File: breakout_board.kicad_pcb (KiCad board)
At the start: 2 copper layers, 30 x 27.6 mm, 27 parts, among them IC2 AS5600-ASOT, J1 Dummy Pins, J2 Debugger, J3 USB_C, U1 STM32F103C8Tx, U2 AMS1117-3.3, Y2 Crystal

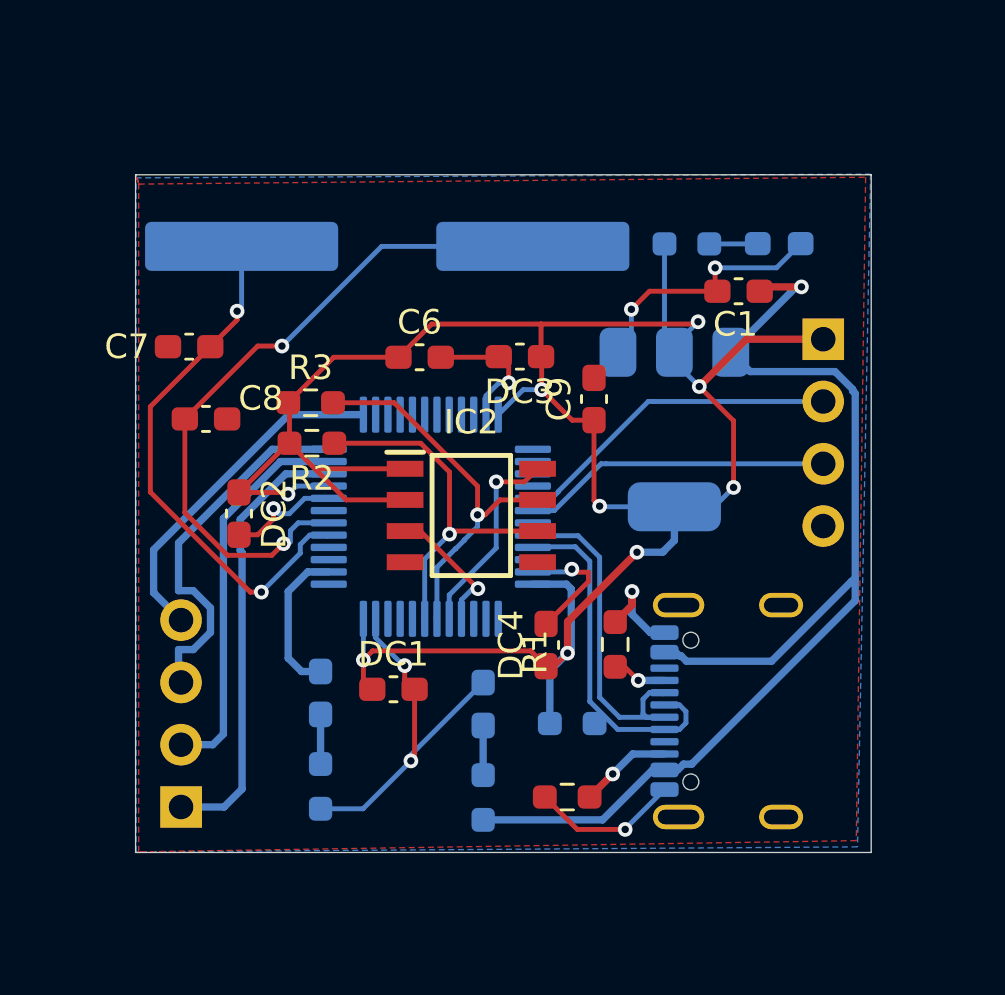
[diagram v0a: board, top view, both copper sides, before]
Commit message: added return vias for ground
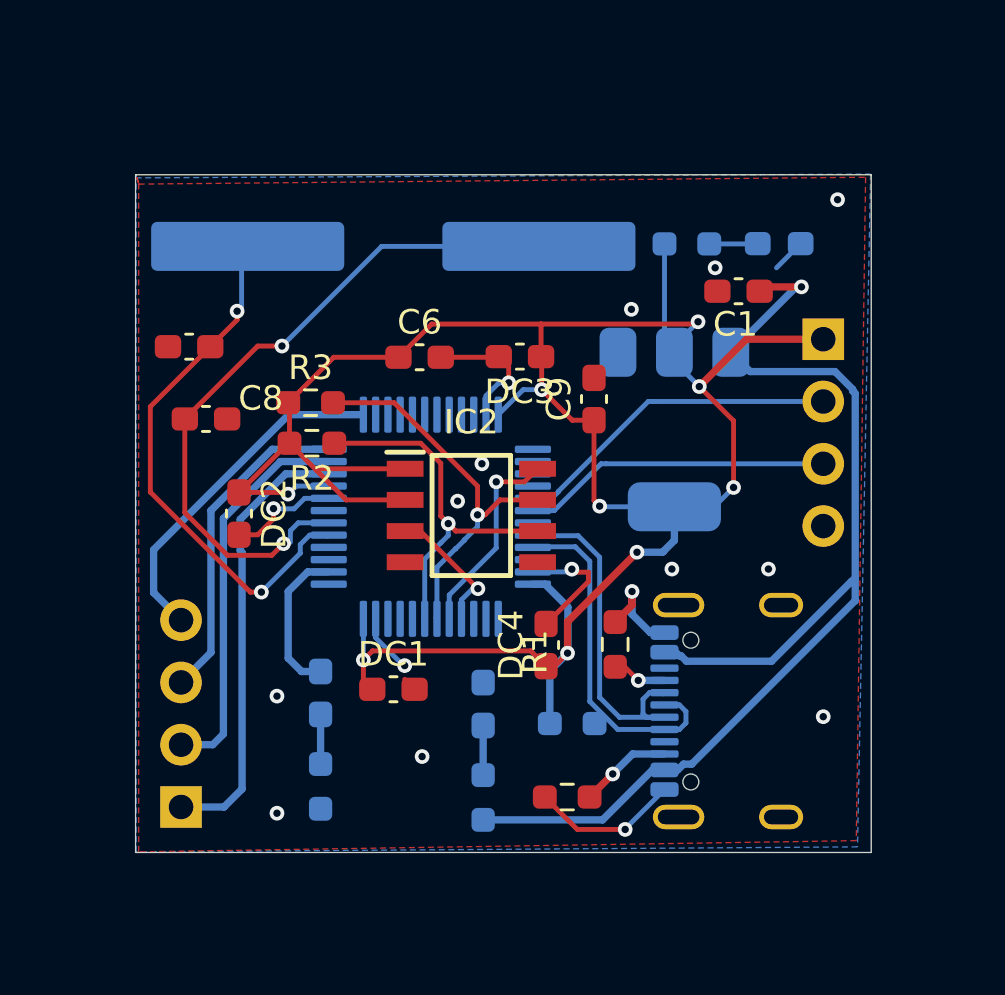
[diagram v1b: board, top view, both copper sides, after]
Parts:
- moved Y2 0.25 mm to (130.0, 68.2)
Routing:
- net GND: track 51.8 -> 30.8 mm, vias 9 -> 17
- net DP3: track 15.2 -> 13.5 mm
- net VDD_c: track 99.2 -> 98.5 mm

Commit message: added mounting holes
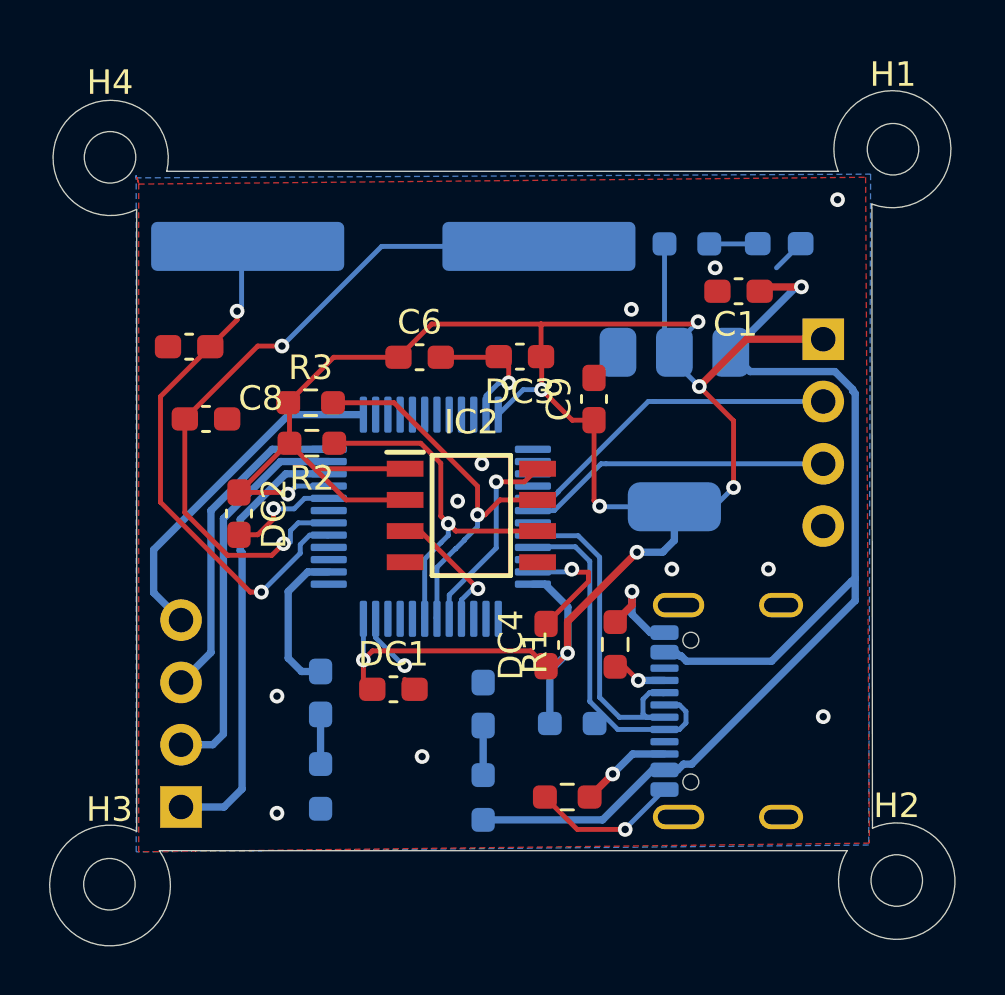
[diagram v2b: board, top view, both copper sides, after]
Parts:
- added H1: MountingHole, MountingHole:MountingHole_2.1mm, F.Cu at (150.4, 64.2)
- added H2: MountingHole, MountingHole:MountingHole_2.1mm, F.Cu at (150.5, 94.1)
- added H3: MountingHole, MountingHole:MountingHole_2.1mm, F.Cu at (118.4, 94.2)
- added H4: MountingHole, MountingHole:MountingHole_2.1mm, F.Cu at (118.4, 64.6)
- J3: value USB_C -> USB_C_Receptacle_USB2.0_16P
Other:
- board size 30 x 27.6 mm -> 36.9 x 34.9 mm

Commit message: silkscreen +minor fixes
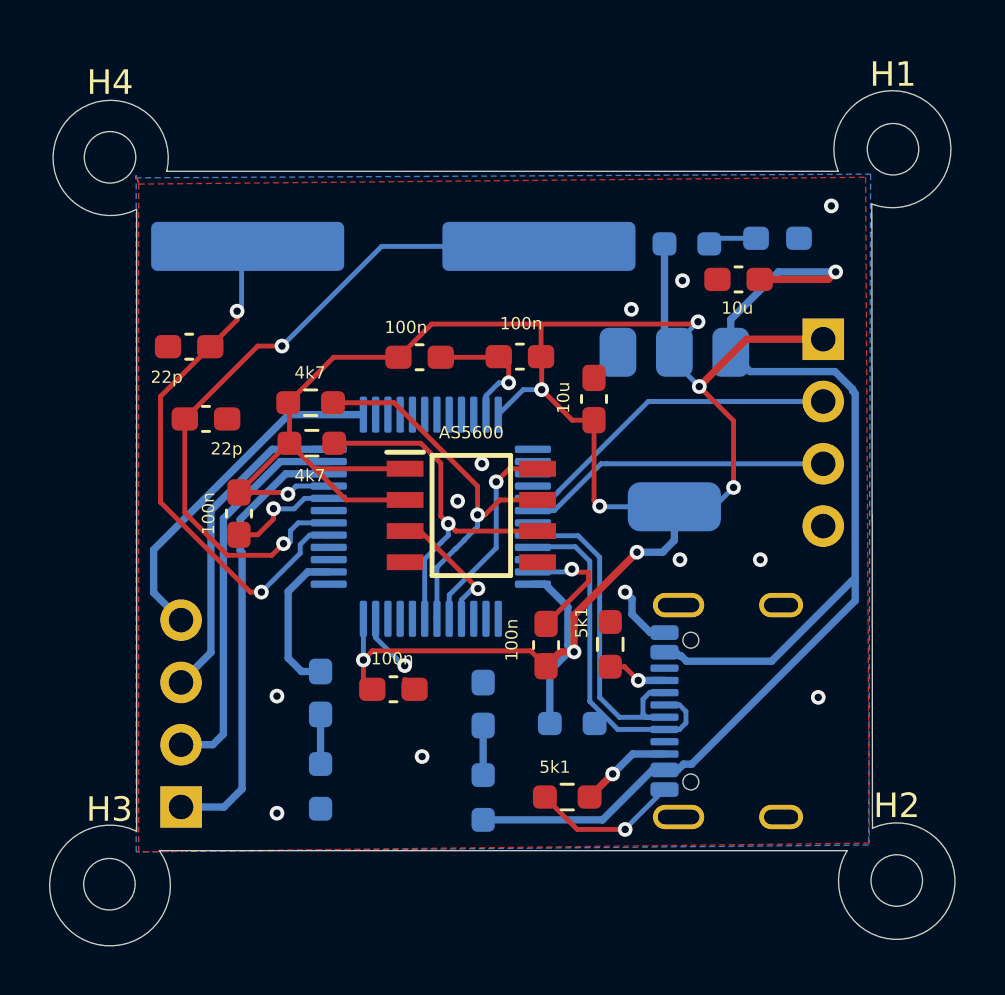
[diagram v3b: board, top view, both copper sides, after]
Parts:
- moved 10u 0.48 mm to (144.1, 69.5)
- moved LED 0.23 mm to (145.7, 67.9)
- moved 5k1 0.20 mm to (138.8, 84.4)
- renumbered DC1 to 100n, C1 to 10u, R6 to 1k, R8 to 1k, R5 to 1k5, C8 to 22p, R3 to 4k7, R1 to 5k1, U2 to AMS1117, IC2 to AS5600, DC2 to DC, DC3 to DC, D3 to LED, Y2 to Oscillator
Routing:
- net VBUS: track 48.2 -> 52.1 mm
- net GND: track 30.8 -> 27.8 mm
- net VDD_c: track 98.5 -> 99.3 mm
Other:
- board text added: "100n"
- board text added: "10u"
- board text added: "1k5"
- board text added: "22p"
- board text added: "4k7"
- board text added: "5k1"
- board text added: "Dummy Pins"
- board text added: "LED"
